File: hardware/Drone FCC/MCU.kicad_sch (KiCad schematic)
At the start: 38 parts, among them SW101 SW RESET, U101 STM32F746ZGTx, Y101 12MHz, Y102 32.768kHz

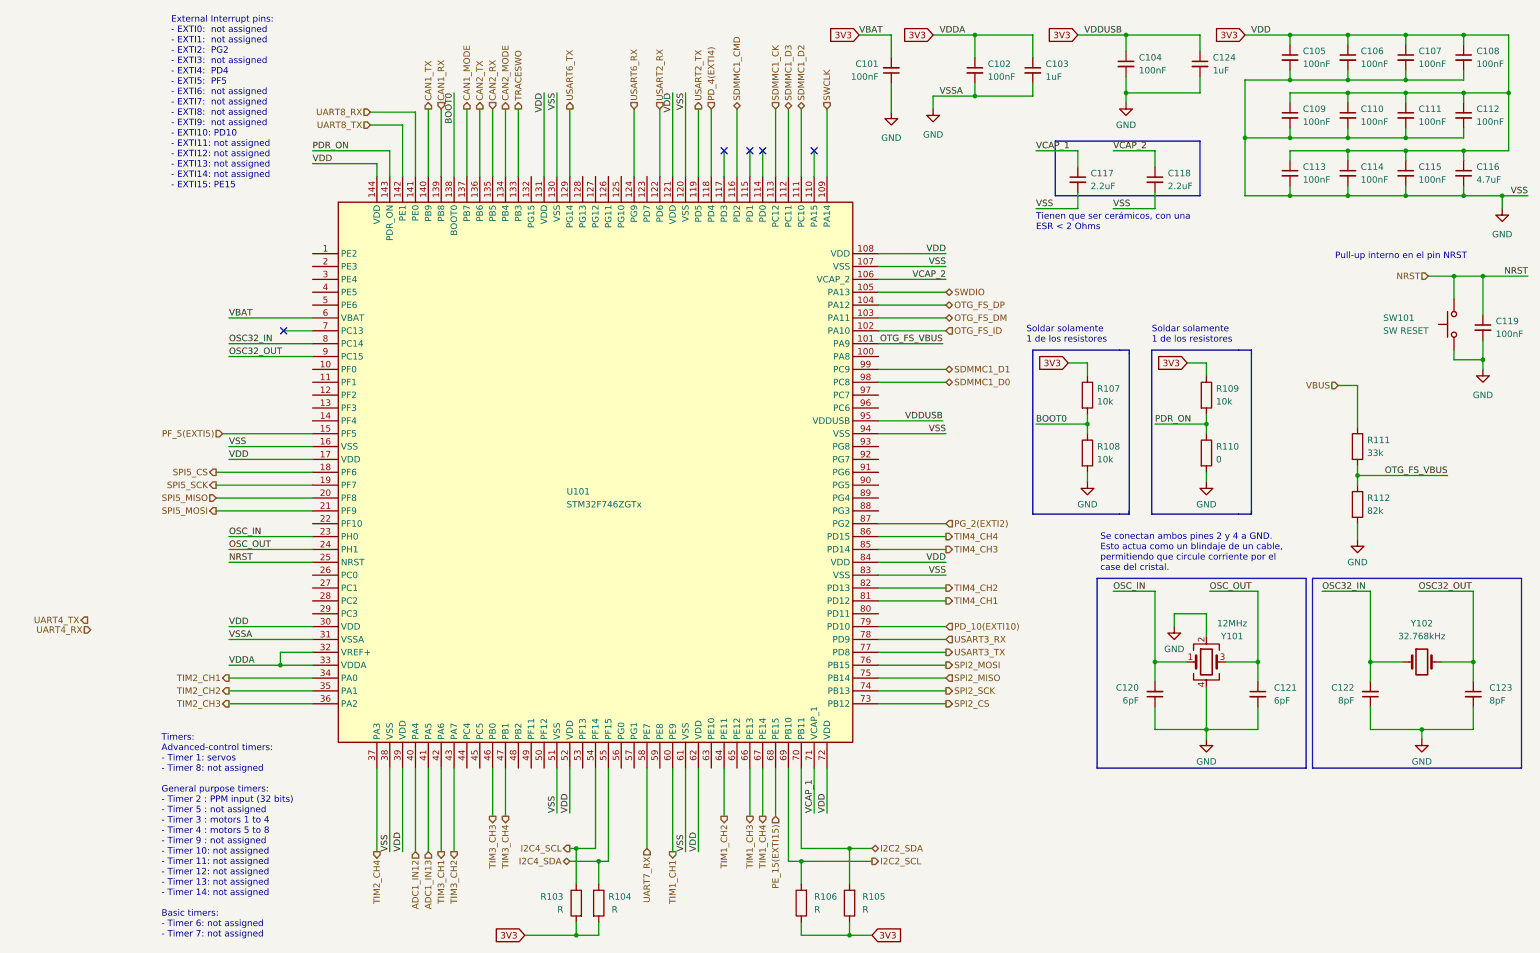
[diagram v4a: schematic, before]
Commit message: positioned components in 100x60 board with incomplete routing
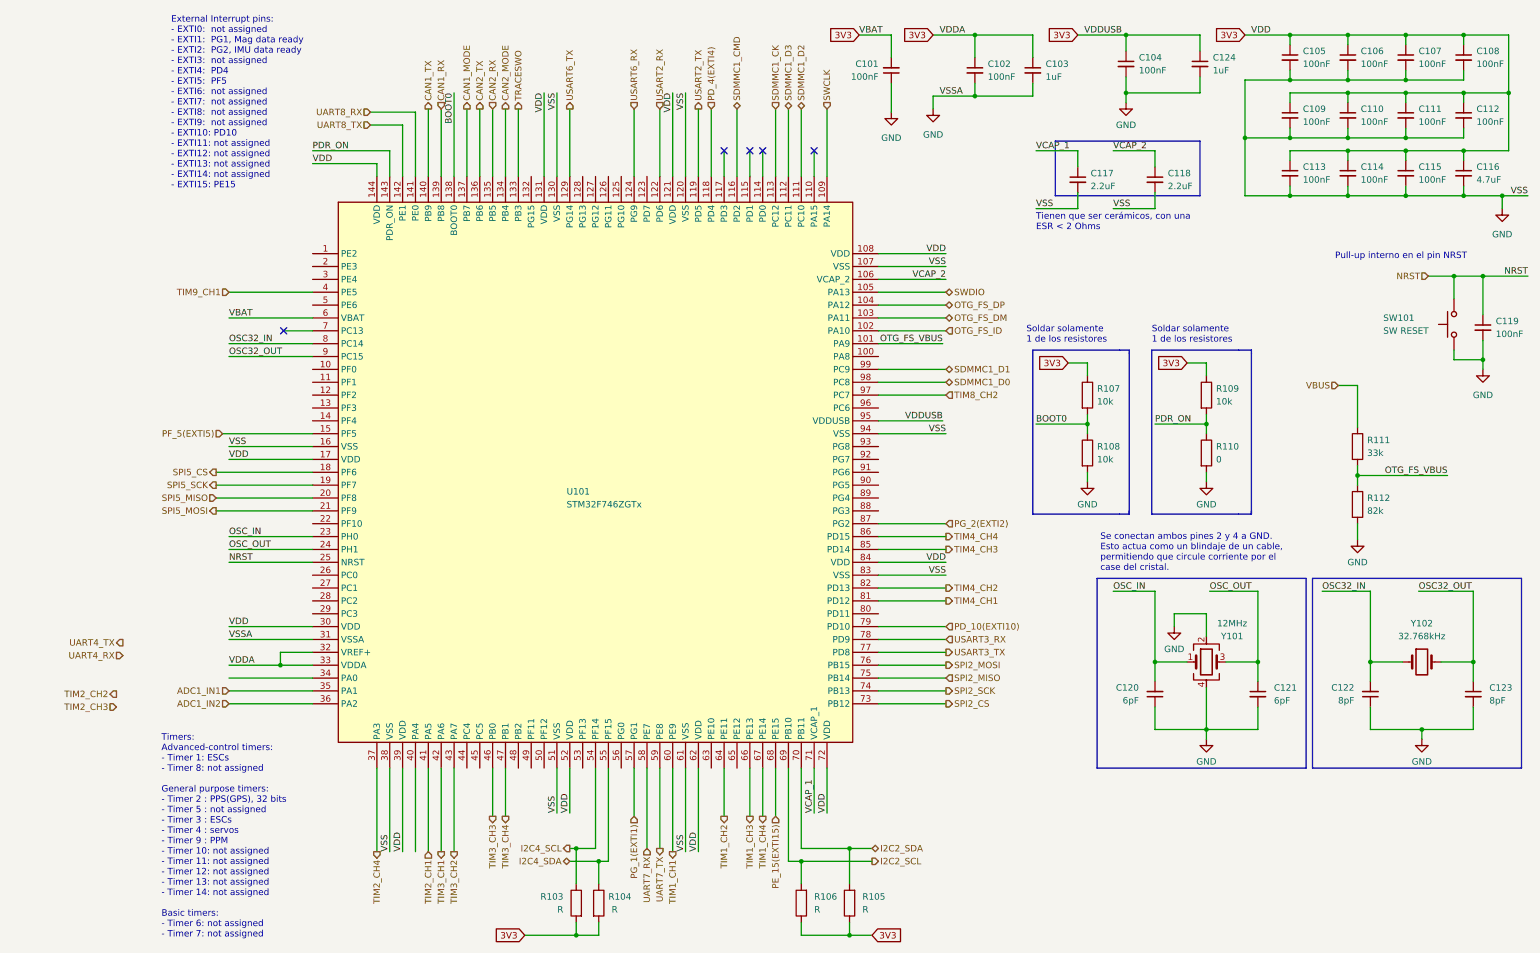
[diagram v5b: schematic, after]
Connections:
- net ADC1_IN13 is gone; now on net TIM2_CH1: U101.41 (PA5)
- net TIM2_CH1: no longer U101.34 (PA0)
- net TIM2_CH2: no longer U101.35 (PA1)
- net TIM2_CH3: no longer U101.36 (PA2)
- net TIM9_CH1: now reaches U101.4 (PE5)
- net PG_1(EXTI1): now reaches U101.57 (PG1)
- net UART7_TX: now reaches U101.59 (PE8)
- net TIM8_CH2: now reaches U101.97 (PC7)
- net ADC1_IN12: no longer names the net of U101.40 (PA4)
- new net ADC1_IN1: U101.35 (PA1)
- new net ADC1_IN2: U101.36 (PA2)
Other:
- note added: "External Interrupt pins: - EXTI0: not assigned - EXTI1: PG1, Mag data ready - EXTI2: PG2, IMU data ready - EXTI3: not assigned - EXTI4: PD4 - EXTI5: PF5 - EXTI6: not assigned - EXTI7: not assigned - EXTI8: not assigned - EXTI9: not assigned - EXTI10: PD10 - EXTI11: not assigned - EXTI12: not assigned - EXTI13: not assigned - EXTI14: not assigned - EXTI15: PE15"
- note added: "Timers: Advanced-control timers: - Timer 1: ESCs - Timer 8: not assigned General purpose timers: - Timer 2 : PPS(GPS), 32 bits - Timer 5 : not assigned - Timer 3 : ESCs - Timer 4 : servos - Timer 9 : PPM - Timer 10: not assigned - Timer 11: not assigned - Timer 12: not assigned - Timer 13: not assigned - Timer 14: not assigned Basic timers: - Timer 6: not assigned - Timer 7: not assigned"
- note removed: "External Interrupt pins: - EXTI0: not assigned - EXTI1: not assigned - EXTI2: PG2 - EXTI3: not assigned - EXTI4: PD4 - EXTI5: PF5 - EXTI6: not assigned - EXTI7: not assigned - EXTI8: not assigned - EXTI9: not assigned - EXTI10: PD10 - EXTI11: not assigned - EXTI12: not assigned - EXTI13: not assigned - EXTI14: not assigned - EXTI15: PE15"
- note removed: "Timers: Advanced-control timers: - Timer 1: servos - Timer 8: not assigned General purpose timers: - Timer 2 : PPM input (32 bits) - Timer 5 : not assigned - Timer 3 : motors 1 to 4 - Timer 4 : motors 5 to 8 - Timer 9 : not assigned - Timer 10: not assigned - Timer 11: not assigned - Timer 12: not assigned - Timer 13: not assigned - Timer 14: not assigned Basic timers: - Timer 6: not assigned - T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"
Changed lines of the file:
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@@
+    (stroke (width 0) (type default) (color 0 0 0 0))
+  )
+  (wire (pts (xy 154.94 88.9) (xy 168.275 88.9))
     (stroke (width 0) (type default) (color 0 0 0 0))
   )
@@
     (stroke (width 0) (type default) (color 0 0 0 0))
   )
+  (wire (pts (xy 26.67 68.58) (xy 43.18 68.58))
+    (stroke (width 0) (type default) (color 0 0 0 0))
+  )
   (wire (pts (xy 139.7 180.975) (xy 153.67 180.975))
     (stroke (width 0) (type default) (color 0 0 0 0))
@@
     (stroke (width 0) (type default) (color 0 0 0 0))
   )
+  (wire (pts (xy 106.68 162.56) (xy 106.68 172.085))
+    (stroke (width 0) (type default) (color 0 0 0 0))
+  )
   (wire (pts (xy 154.94 78.74) (xy 167.64 78.74))
     (stroke (width 0) (type default) (color 0 0 0 0))
@@
   )
   (wire (pts (xy 247.65 49.53) (xy 259.08 49.53))
+    (stroke (width 0) (type default) (color 0 0 0 0))
+  )
+  (wire (pts (xy 111.76 178.435) (xy 111.76 162.56))
     (stroke (width 0) (type default) (color 0 0 0 0))
   )
@@
     (effects (font (size 1.27 1.27)) (justify left bottom))
   )
-  (text "External Interrupt pins:\n- EXTI0:  not assigned\n- EXTI1:  not assigned\n- EXTI2:  PG2\n- EXTI3:  not assigned\n- EXTI4:  PD4\n- EXTI5:  PF5\n- EXTI6:  not assigned\n- EXTI7:  not assigned\n- EXTI8:  not assigned\n- EXTI9:  not assigned\n- EXTI10: PD10\n- EXTI11: not assigned\n- EXTI12: not assigned\n- EXTI13: not assigned\n- EXTI14: not assigned\n- EXTI15: PE15"
+  (text "External Interrupt pins:\n- EXTI0:  not assigned\n- EXTI1:  PG1, Mag data ready\n- EXTI2:  PG2, IMU data ready\n- EXTI3:  not assigned\n- EXTI4:  PD4\n- EXTI5:  PF5\n- EXTI6:  not assigned\n- EXTI7:  not assigned\n- EXTI8:  not assigned\n- EXTI9:  not assigned\n- EXTI10: PD10\n- EXTI11: not assigned\n- EXTI12: not assigned\n- EXTI13: not assigned\n- EXTI14: not assigned\n- EXTI15: PE15"
     (at 15.24 48.26 0)
     (effects (font (size 1.27 1.27)) (justify left bottom))
@@
     (effects (font (size 1.27 1.27)) (justify left bottom))
   )
-  (text "Timers:\nAdvanced-control timers:\n- Timer 1: servos\n- Timer 8: not assigned\n\nGeneral purpose timers:\n- Timer 2 : PPM input (32 bits)\n- Timer 5 : not assigned\n- Timer 3 : motors 1 to 4\n- Timer 4 : motors 5 to 8\n- Timer 9 : not assigned\n- Timer 10: not assigned\n- Timer 11: not assigned\n- Timer 12: not assigned\n- Timer 13: not assigned\n- Timer 14: not assigned\n\nBasic timers:\n- Timer 6: not assigned\n- Timer 7: not assigned"
+  (text "Timers:\nAdvanced-control timers:\n- Timer 1: ESCs\n- Timer 8: not assigned\n\nGeneral purpose timers:\n- Timer 2 : PPS(GPS), 32 bits\n- Timer 5 : not assigned\n- Timer 3 : ESCs\n- Timer 4 : servos\n- Timer 9 : PPM\n- Timer 10: not assigned\n- Timer 11: not assigned\n- Timer 12: not assigned\n- Timer 13: not assigned\n- Timer 14: not assigned\n\nBasic timers:\n- Timer 6: not assigned\n- Timer 7: not assigned"
     (at 13.335 196.215 0)
     (effects (font (size 1.27 1.27)) (justify left bottom))
@@
     (effects (font (size 1.27 1.27)) (justify left))
   )
-  (hierarchical_label "ADC1_IN13" (shape input) (at 66.04 179.07 270)
-    (effects (font (size 1.27 1.27)) (justify right))
-  )
-  (hierarchical_label "TIM2_CH1" (shape output) (at 26.67 144.78 180)
+  (hierarchical_label "ADC1_IN2" (shape input) (at 26.67 149.86 180)
+    (effects (font (size 1.27 1.27)) (justify right))
+  )
+  (hierarchical_label "TIM2_CH1" (shape input) (at 66.04 179.07 270)
     (effects (font (size 1.27 1.27)) (justify right))
   )
@@
     (effects (font (size 1.27 1.27)) (justify right))
   )
+  (hierarchical_label "TIM8_CH2" (shape input) (at 168.275 88.9 0)
+    (effects (font (size 1.27 1.27)) (justify left))
+  )
   (hierarchical_label "TIM4_CH4" (shape output) (at 168.275 116.84 0)
     (effects (font (size 1.27 1.27)) (justify left))
@@
     (effects (font (size 1.27 1.27)) (justify left))
   )
-  (hierarchical_label "ADC1_IN12" (shape input) (at 63.5 179.07 270)
+  (hierarchical_label "ADC1_IN1" (shape input) (at 26.67 147.32 180)
     (effects (font (size 1.27 1.27)) (justify right))
   )
@@
     (effects (font (size 1.27 1.27)) (justify left))
   )
-  (hierarchical_label "UART4_TX" (shape output) (at -1.27 133.35 180)
+  (hierarchical_label "UART4_TX" (shape output) (at 5.715 137.795 180)
     (effects (font (size 1.27 1.27)) (justify right))
   )
@@
     (effects (font (size 1.27 1.27)) (justify left))
   )
+  (hierarchical_label "PG_1(EXTI1)" (shape input) (at 106.68 172.085 270)
+    (effects (font (size 1.27 1.27)) (justify right))
+  )
   (hierarchical_label "PE_15(EXTI15)" (shape input) (at 134.62 172.085 270)
     (effects (font (size 1.27 1.27)) (justify right))
@@
     (effects (font (size 1.27 1.27)) (justify right))
   )
-  (hierarchical_label "TIM2_CH3" (shape output) (at 26.67 149.86 180)
+  (hierarchical_label "TIM9_CH1" (shape input) (at 26.67 68.58 180)
+    (effects (font (size 1.27 1.27)) (justify right))
+  )
+  (hierarchical_label "TIM2_CH3" (shape input) (at 4.445 150.495 180)
     (effects (font (size 1.27 1.27)) (justify right))
   )
@@
     (effects (font (size 1.27 1.27)) (justify right))
   )
-  (hierarchical_label "TIM2_CH2" (shape output) (at 26.67 147.32 180)
+  (hierarchical_label "TIM2_CH2" (shape output) (at 4.445 147.955 180)
     (effects (font (size 1.27 1.27)) (justify right))
   )
@@
     (effects (font (size 1.27 1.27)) (justify left))
   )
-  (hierarchical_label "UART4_RX" (shape input) (at -0.635 135.255 180)
-    (effects (font (size 1.27 1.27)) (justify right))
-  )
+  (hierarchical_label "UART7_TX" (shape output) (at 111.76 178.435 270)
+    (effects (font (size 1.27 1.27)) (justify right))
+  )
+  (hierarchical_label "UART4_RX" (shape input) (at 5.715 140.335 180)
+    (effects (font (size 1.27 1.27)) (justify right))
+  )

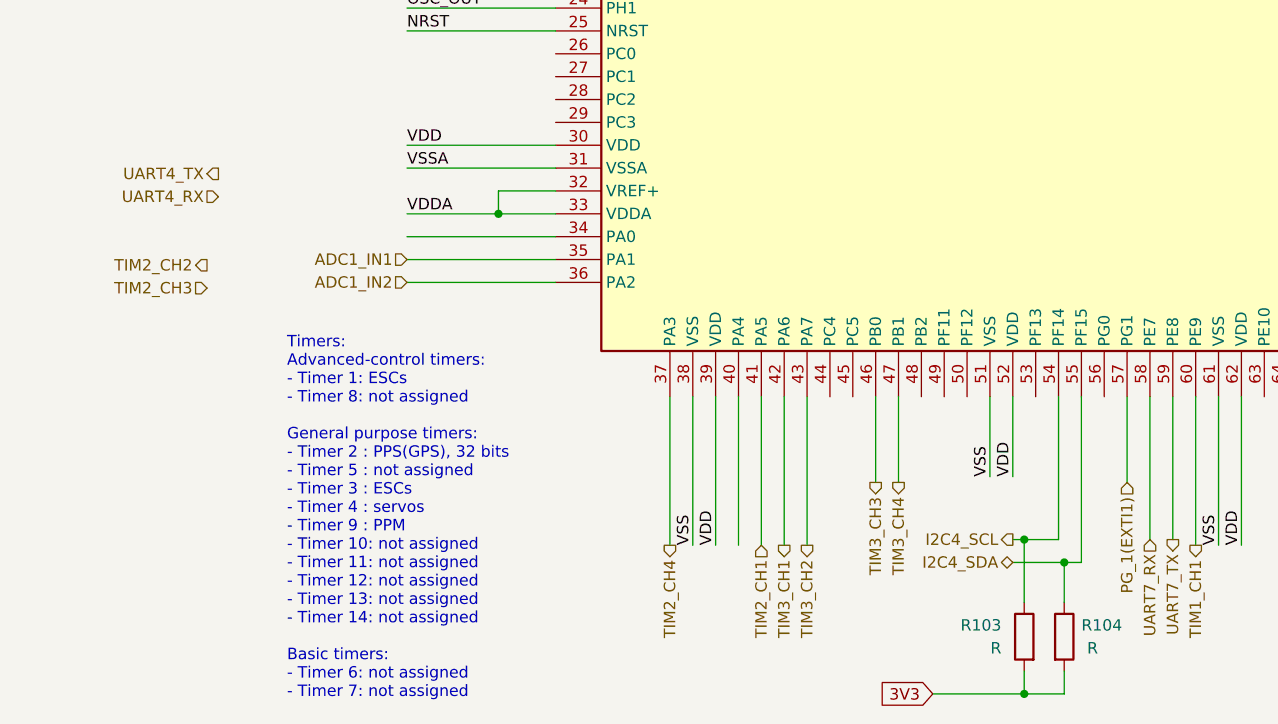
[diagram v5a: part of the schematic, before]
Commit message: todo: route SWD connector
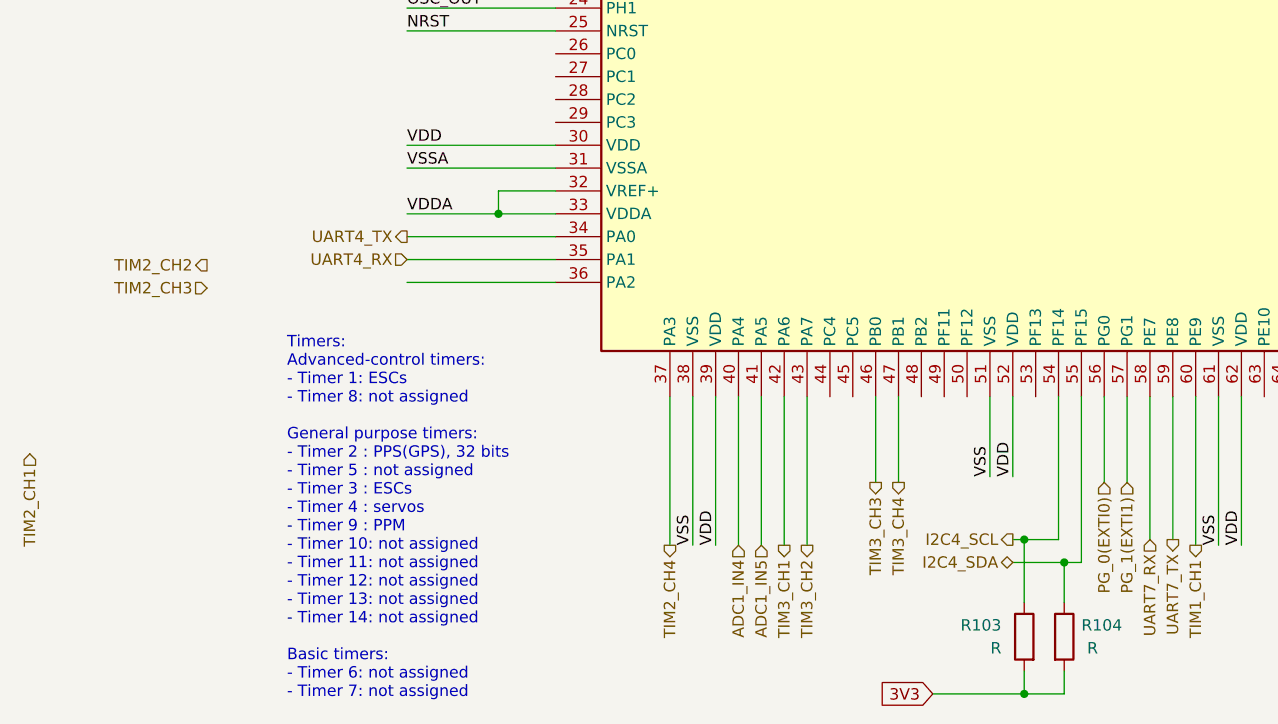
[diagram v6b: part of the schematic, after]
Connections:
- net ADC1_IN1 is gone; now on net UART4_RX: U101.35 (PA1)
- net TIM2_CH1: no longer U101.41 (PA5)
- net UART4_TX: now also U101.34 (PA0)
- net ADC1_IN4: now reaches U101.40 (PA4)
- net PG_0(EXTI0): now reaches U101.56 (PG0)
- net ADC1_IN2: no longer names the net of U101.36 (PA2)
- new net ADC1_IN5: U101.41 (PA5)
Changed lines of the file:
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@@
+    (stroke (width 0) (type default) (color 0 0 0 0))
+  )
+  (wire (pts (xy 104.14 162.56) (xy 104.14 172.085))
     (stroke (width 0) (type default) (color 0 0 0 0))
   )
@@
     (effects (font (size 1.27 1.27)) (justify left))
   )
-  (hierarchical_label "ADC1_IN2" (shape input) (at 26.67 149.86 180)
-    (effects (font (size 1.27 1.27)) (justify right))
-  )
-  (hierarchical_label "TIM2_CH1" (shape input) (at 66.04 179.07 270)
+  (hierarchical_label "ADC1_IN5" (shape input) (at 66.04 179.07 270)
+    (effects (font (size 1.27 1.27)) (justify right))
+  )
+  (hierarchical_label "TIM2_CH1" (shape input) (at -15.24 168.91 270)
+    (effects (font (size 1.27 1.27)) (justify right))
+  )
+  (hierarchical_label "PG_0(EXTI0)" (shape input) (at 104.14 172.085 270)
     (effects (font (size 1.27 1.27)) (justify right))
   )
@@
     (effects (font (size 1.27 1.27)) (justify left))
   )
-  (hierarchical_label "ADC1_IN1" (shape input) (at 26.67 147.32 180)
+  (hierarchical_label "ADC1_IN4" (shape input) (at 63.5 179.07 270)
     (effects (font (size 1.27 1.27)) (justify right))
   )
@@
     (effects (font (size 1.27 1.27)) (justify left))
   )
-  (hierarchical_label "UART4_TX" (shape output) (at 5.715 137.795 180)
+  (hierarchical_label "UART4_TX" (shape output) (at 26.67 144.78 180)
     (effects (font (size 1.27 1.27)) (justify right))
   )
@@
     (effects (font (size 1.27 1.27)) (justify right))
   )
-  (hierarchical_label "UART4_RX" (shape input) (at 5.715 140.335 180)
-    (effects (font (size 1.27 1.27)) (justify right))
-  )
+  (hierarchical_label "UART4_RX" (shape input) (at 26.67 147.32 180)
+    (effects (font (size 1.27 1.27)) (justify right))
+  )

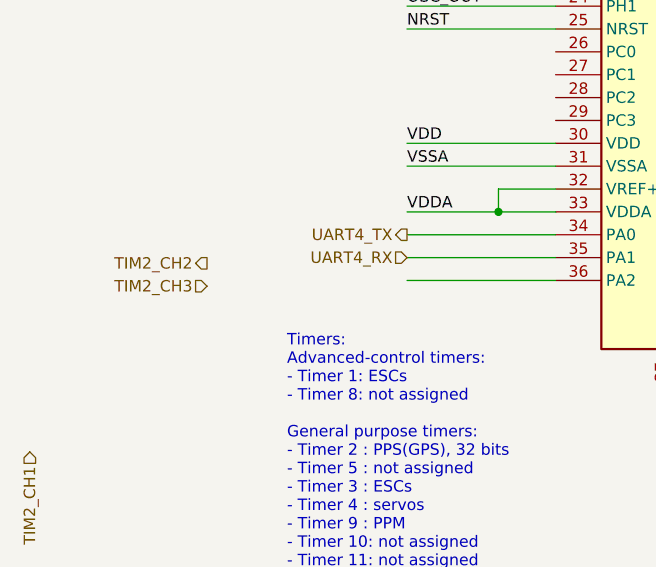
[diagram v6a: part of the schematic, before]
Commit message: included SWD header in routing
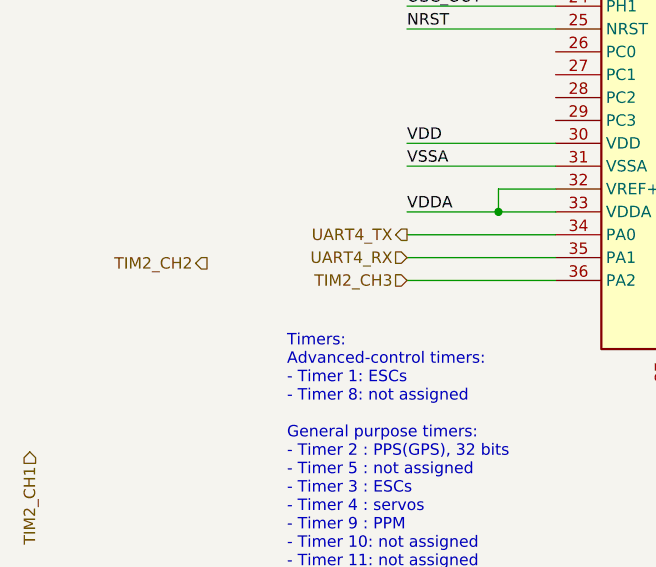
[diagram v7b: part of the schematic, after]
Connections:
- net TIM2_CH3: now also U101.36 (PA2)
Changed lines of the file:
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@@
     (effects (font (size 1.27 1.27)) (justify right))
   )
-  (hierarchical_label "TIM2_CH3" (shape input) (at 4.445 150.495 180)
+  (hierarchical_label "TIM2_CH3" (shape input) (at 26.67 149.86 180)
     (effects (font (size 1.27 1.27)) (justify right))
   )
